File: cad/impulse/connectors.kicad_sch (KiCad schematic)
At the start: 21 parts, among them J1 Screw_Terminal_01x02, J2 Screw_Terminal_01x02, J3 Screw_Terminal_01x02, J4 Screw_Terminal_01x02, J5 Screw_Terminal_01x02, Q1 Q_NMOS_DGS, Q3 Q_NMOS_DGS, Q4 Q_NMOS_DGS, Q5 Q_NMOS_DGS

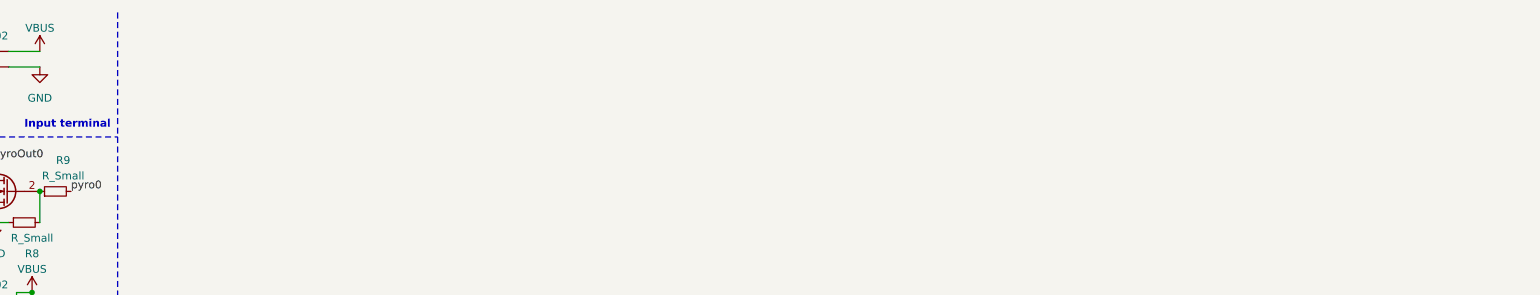
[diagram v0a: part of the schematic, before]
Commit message: Started Working on sensors. Made connectors for servos.
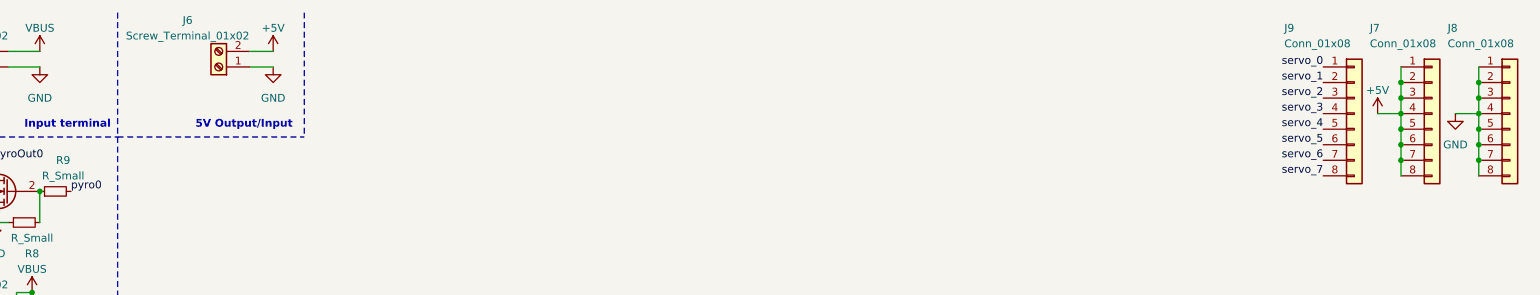
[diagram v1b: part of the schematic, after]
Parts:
- added J6: Screw_Terminal_01x02, symbol Connector:Screw_Terminal_01x02
- added J7, J8, J9: Conn_01x08, Connector_RJ:RJ45_Amphenol_54602-x08_Horizontal, symbol Connector_Generic:Conn_01x08
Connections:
- net GND: now also J6.1 (Pin_1), J8.1 (Pin_1), J8.2 (Pin_2), J8.3 (Pin_3), J8.4 (Pin_4), J8.5 (Pin_5), J8.6 (Pin_6), J8.7 (Pin_7), J8.8 (Pin_8)
- new net +5V: J6.2 (Pin_2), J7.1 (Pin_1), J7.2 (Pin_2), J7.3 (Pin_3), J7.4 (Pin_4), J7.5 (Pin_5), J7.6 (Pin_6), J7.7 (Pin_7), J7.8 (Pin_8)
- new net servo_0: J9.1 (Pin_1)
- new net servo_1: J9.2 (Pin_2)
- new net servo_2: J9.3 (Pin_3)
- new net servo_3: J9.4 (Pin_4)
- new net servo_4: J9.5 (Pin_5)
- new net servo_5: J9.6 (Pin_6)
- new net servo_6: J9.7 (Pin_7)
- new net servo_7: J9.8 (Pin_8)
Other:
- note added: "5V Output/Input"

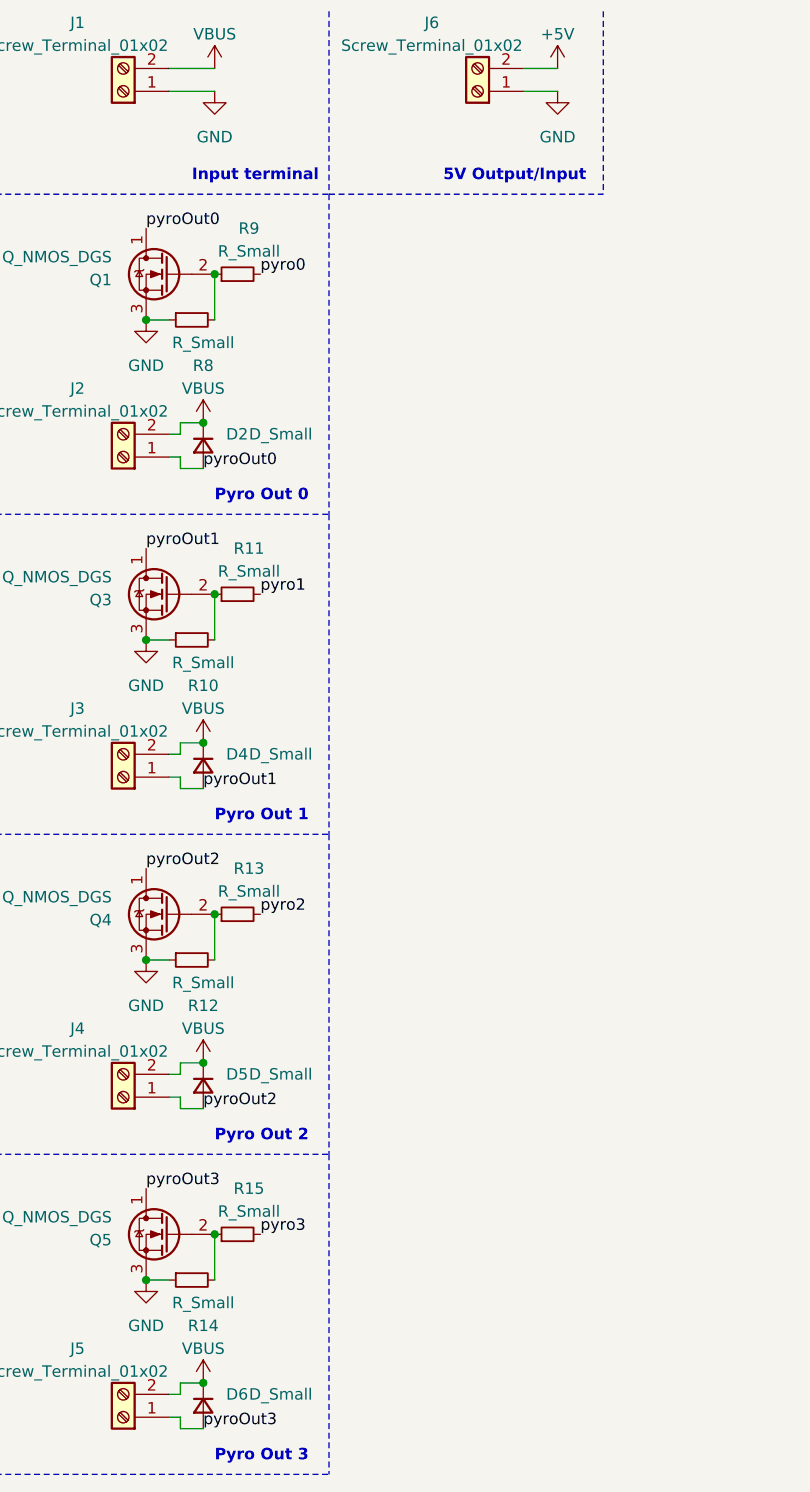
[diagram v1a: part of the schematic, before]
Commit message: Added IMU, button and led. Moved things around.
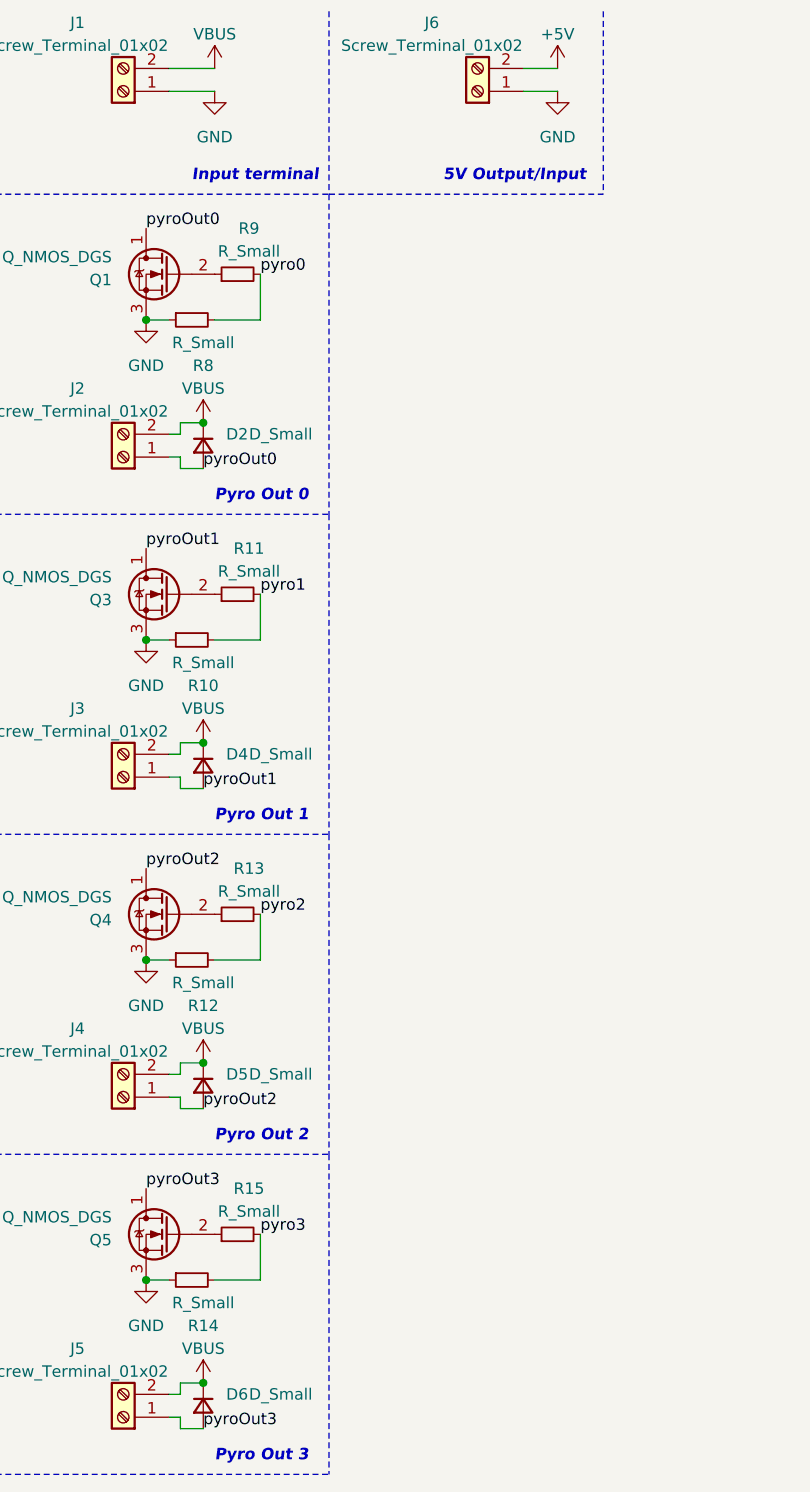
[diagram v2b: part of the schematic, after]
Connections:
- net pyro0: now also R8.2
- net pyro1: now also R10.2
- net pyro2: now also R12.2
- net pyro3: now also R14.2
- net at Q4.2 (G), R13.1: no longer R12.2
- net at Q3.2 (G), R11.1: no longer R10.2
- net at Q1.2 (G), R9.1: no longer R8.2
- net at Q5.2 (G), R15.1: no longer R14.2
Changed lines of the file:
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@@
   (junction (at 260.35 34.29) (diameter 0) (color 0 0 0 0)
   )
-  (junction (at 38.1 113.03) (diameter 0) (color 0 0 0 0)
-  )
   (junction (at 36.83 129.54) (diameter 0) (color 0 0 0 0)
   )
   (junction (at 260.35 31.75) (diameter 0) (color 0 0 0 0)
   )
-  (junction (at 38.1 41.91) (diameter 0) (color 0 0 0 0)
-  )
   (junction (at 36.83 58.42) (diameter 0) (color 0 0 0 0)
   )
-  (junction (at 38.1 77.47) (diameter 0) (color 0 0 0 0)
-  )
   (junction (at 273.05 36.83) (diameter 0) (color 0 0 0 0)
   )
@@
   (junction (at 273.05 31.75) (diameter 0) (color 0 0 0 0)
   )
-  (junction (at 38.1 148.59) (diameter 0) (color 0 0 0 0)
-  )
   (junction (at 260.35 26.67) (diameter 0) (color 0 0 0 0)
   )
@@
     (stroke (width 0) (type default))
   )
-  (wire (pts (xy 38.1 77.47) (xy 38.1 82.55))
-    (stroke (width 0) (type default))
-  )
   (wire (pts (xy 33.02 95.25) (xy 34.29 95.25))
     (stroke (width 0) (type default))
@@
     (stroke (width 0) (type default))
   )
+  (wire (pts (xy 43.18 46.99) (xy 43.18 41.91))
+    (stroke (width 0) (type default))
+  )
   (polyline (pts (xy 50.8 12.7) (xy 50.8 33.02))
     (stroke (width 0) (type dash))
@@
     (stroke (width 0) (type default))
   )
+  (wire (pts (xy 43.18 153.67) (xy 43.18 148.59))
+    (stroke (width 0) (type default))
+  )
   (wire (pts (xy 260.35 26.67) (xy 260.35 29.21))
     (stroke (width 0) (type default))
@@
     (stroke (width 0) (type default))
   )
+  (wire (pts (xy 43.18 118.11) (xy 43.18 113.03))
+    (stroke (width 0) (type default))
+  )
   (wire (pts (xy 33.02 168.91) (xy 34.29 168.91))
     (stroke (width 0) (type default))
   )
-  (wire (pts (xy 38.1 41.91) (xy 38.1 46.99))
-    (stroke (width 0) (type default))
-  )
   (wire (pts (xy 34.29 166.37) (xy 34.29 165.1))
     (stroke (width 0) (type default))
@@
     (stroke (width 0) (type default))
   )
+  (wire (pts (xy 38.1 118.11) (xy 43.18 118.11))
+    (stroke (width 0) (type default))
+  )
   (wire (pts (xy 34.29 97.79) (xy 34.29 99.06))
     (stroke (width 0) (type default))
@@
     (stroke (width 0) (type default))
   )
+  (wire (pts (xy 38.1 153.67) (xy 43.18 153.67))
+    (stroke (width 0) (type default))
+  )
   (wire (pts (xy 273.05 29.21) (xy 273.05 31.75))
     (stroke (width 0) (type default))
@@
     (stroke (width 0) (type default))
   )
+  (wire (pts (xy 43.18 82.55) (xy 43.18 77.47))
+    (stroke (width 0) (type default))
+  )
+  (wire (pts (xy 38.1 82.55) (xy 43.18 82.55))
+    (stroke (width 0) (type default))
+  )
   (wire (pts (xy 269.24 29.21) (xy 273.05 29.21))
     (stroke (width 0) (type default))
@@
     (stroke (width 0) (type default))
   )
-  (wire (pts (xy 38.1 113.03) (xy 38.1 118.11))
-    (stroke (width 0) (type default))
-  )
   (wire (pts (xy 34.29 62.23) (xy 34.29 63.5))
     (stroke (width 0) (type default))
@@
     (stroke (width 0) (type dash))
   )
-  (wire (pts (xy 38.1 148.59) (xy 38.1 153.67))
-    (stroke (width 0) (type default))
-  )
   (polyline (pts (xy 50.8 68.58) (xy 50.8 104.14))
     (stroke (width 0) (type dash))
@@
     (stroke (width 0) (type default))
   )
+  (wire (pts (xy 38.1 46.99) (xy 43.18 46.99))
+    (stroke (width 0) (type default))
+  )
   (wire (pts (xy 33.02 82.55) (xy 30.48 82.55))
     (stroke (width 0) (type default))
@@
   )
   (text "Pyro Out 1" (at 38.1 102.87 0)
-    (effects (font (size 1.27 1.27) (thickness 0.254) bold) (justify left bottom))
+    (effects (font (size 1.27 1.27) (thickness 0.254) bold italic) (justify left bottom))
   )
   (text "Pyro Out 0" (at 38.1 67.31 0)
-    (effects (font (size 1.27 1.27) (thickness 0.254) bold) (justify left bottom))
+    (effects (font (size 1.27 1.27) (thickness 0.254) bold italic) (justify left bottom))
   )
   (text "Pyro Out 3" (at 38.1 173.99 0)
-    (effects (font (size 1.27 1.27) (thickness 0.254) bold) (justify left bottom))
+    (effects (font (size 1.27 1.27) (thickness 0.254) bold italic) (justify left bottom))
   )
   (text "Pyro Out 2" (at 38.1 138.43 0)
-    (effects (font (size 1.27 1.27) (thickness 0.254) bold) (justify left bottom))
+    (effects (font (size 1.27 1.27) (thickness 0.254) bold italic) (justify left bottom))
   )
   (text "5V Output/Input" (at 63.5 31.75 0)
-    (effects (font (size 1.27 1.27) (thickness 0.254) bold) (justify left bottom))
+    (effects (font (size 1.27 1.27) (thickness 0.254) bold italic) (justify left bottom))
   )
   (text "Input terminal" (at 35.56 31.75 0)
-    (effects (font (size 1.27 1.27) (thickness 0.254) bold) (justify left bottom))
+    (effects (font (size 1.27 1.27) (thickness 0.254) bold italic) (justify left bottom))
   )
   (label "servo_6" (at 247.65 36.83 180) (fields_autoplaced)

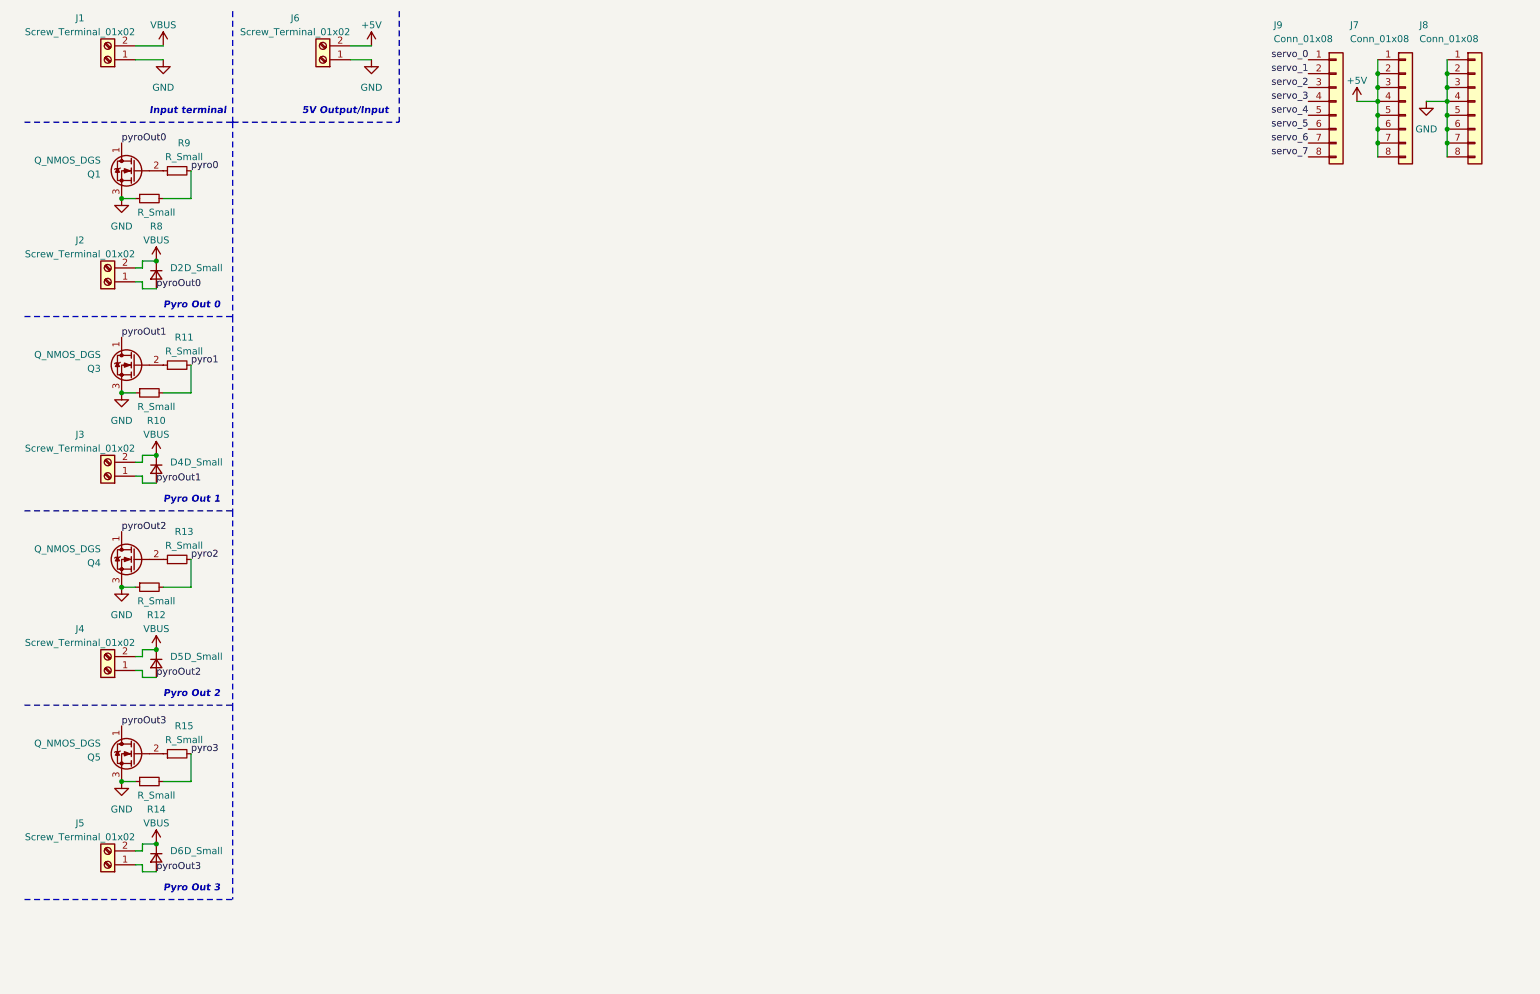
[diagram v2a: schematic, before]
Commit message: Transitioned to global labels when needed.
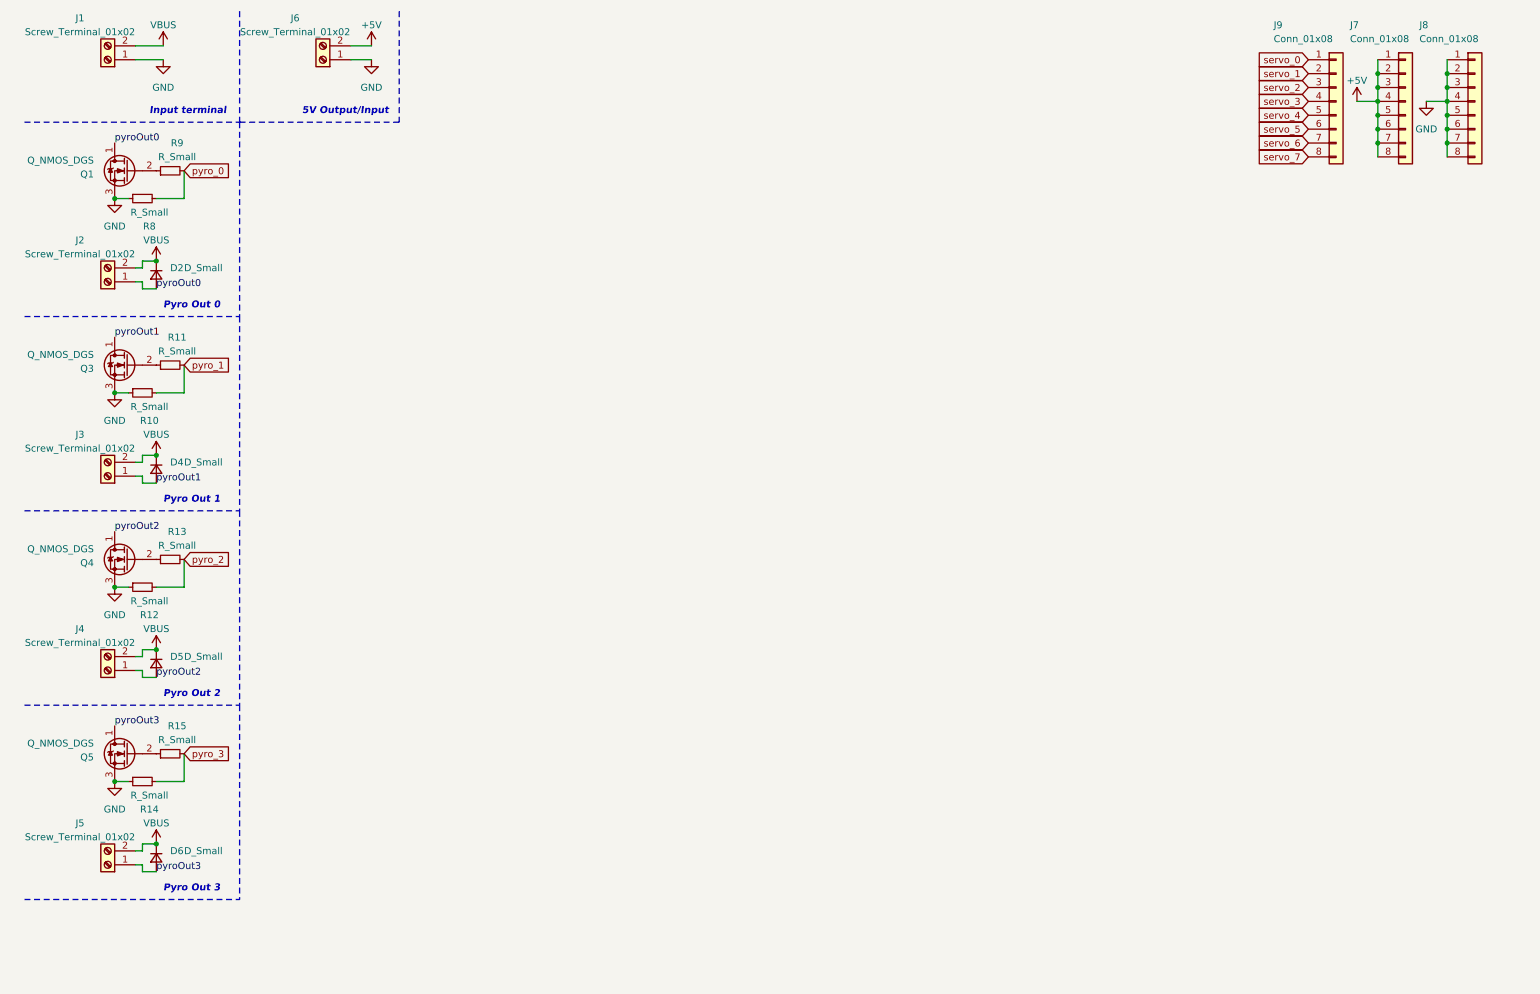
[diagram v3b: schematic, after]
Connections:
- net pyro0 renamed pyro_0
- net pyro1 renamed pyro_1
- net pyro2 renamed pyro_2
- net pyro3 renamed pyro_3
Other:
- moved on the sheet: Q1, Q3, Q4, Q5, R10, R11, R12, R13, R14, R15, R8, R9
